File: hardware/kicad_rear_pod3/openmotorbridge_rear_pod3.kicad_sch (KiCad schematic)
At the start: 0 parts

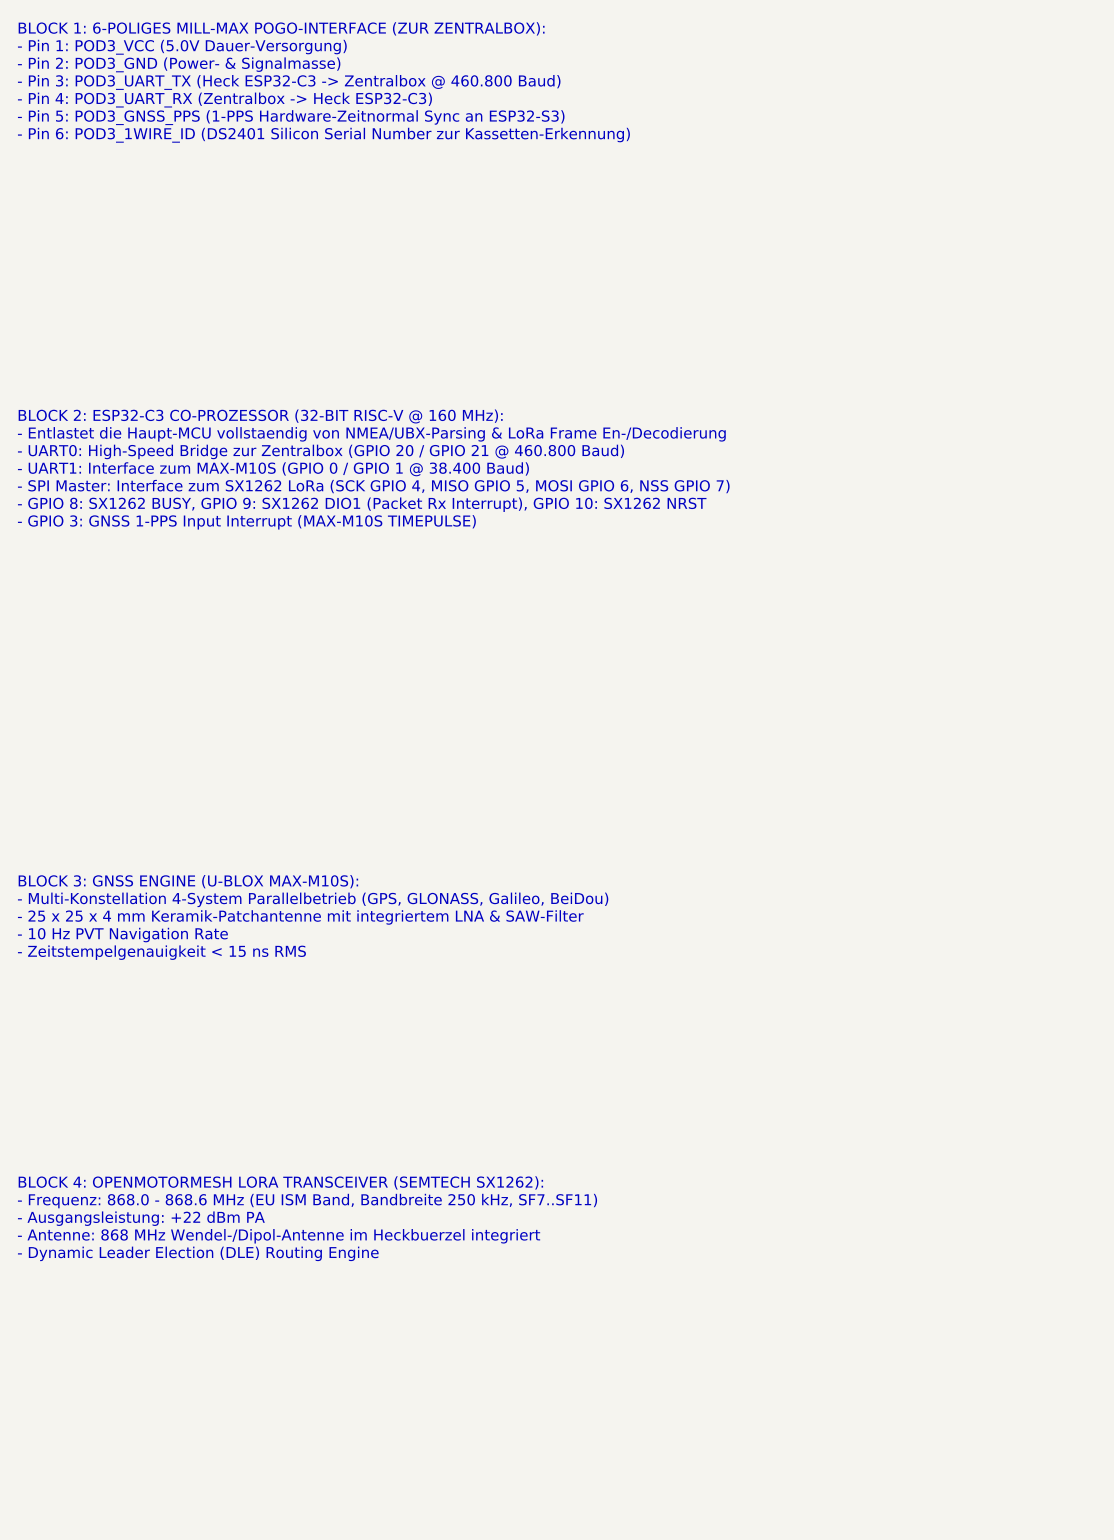
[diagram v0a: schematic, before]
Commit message: feat: Add Adaptive Tiered QoS, Dual-PHY OMM, Dead Reckoning, Actioncam Remote & i18n
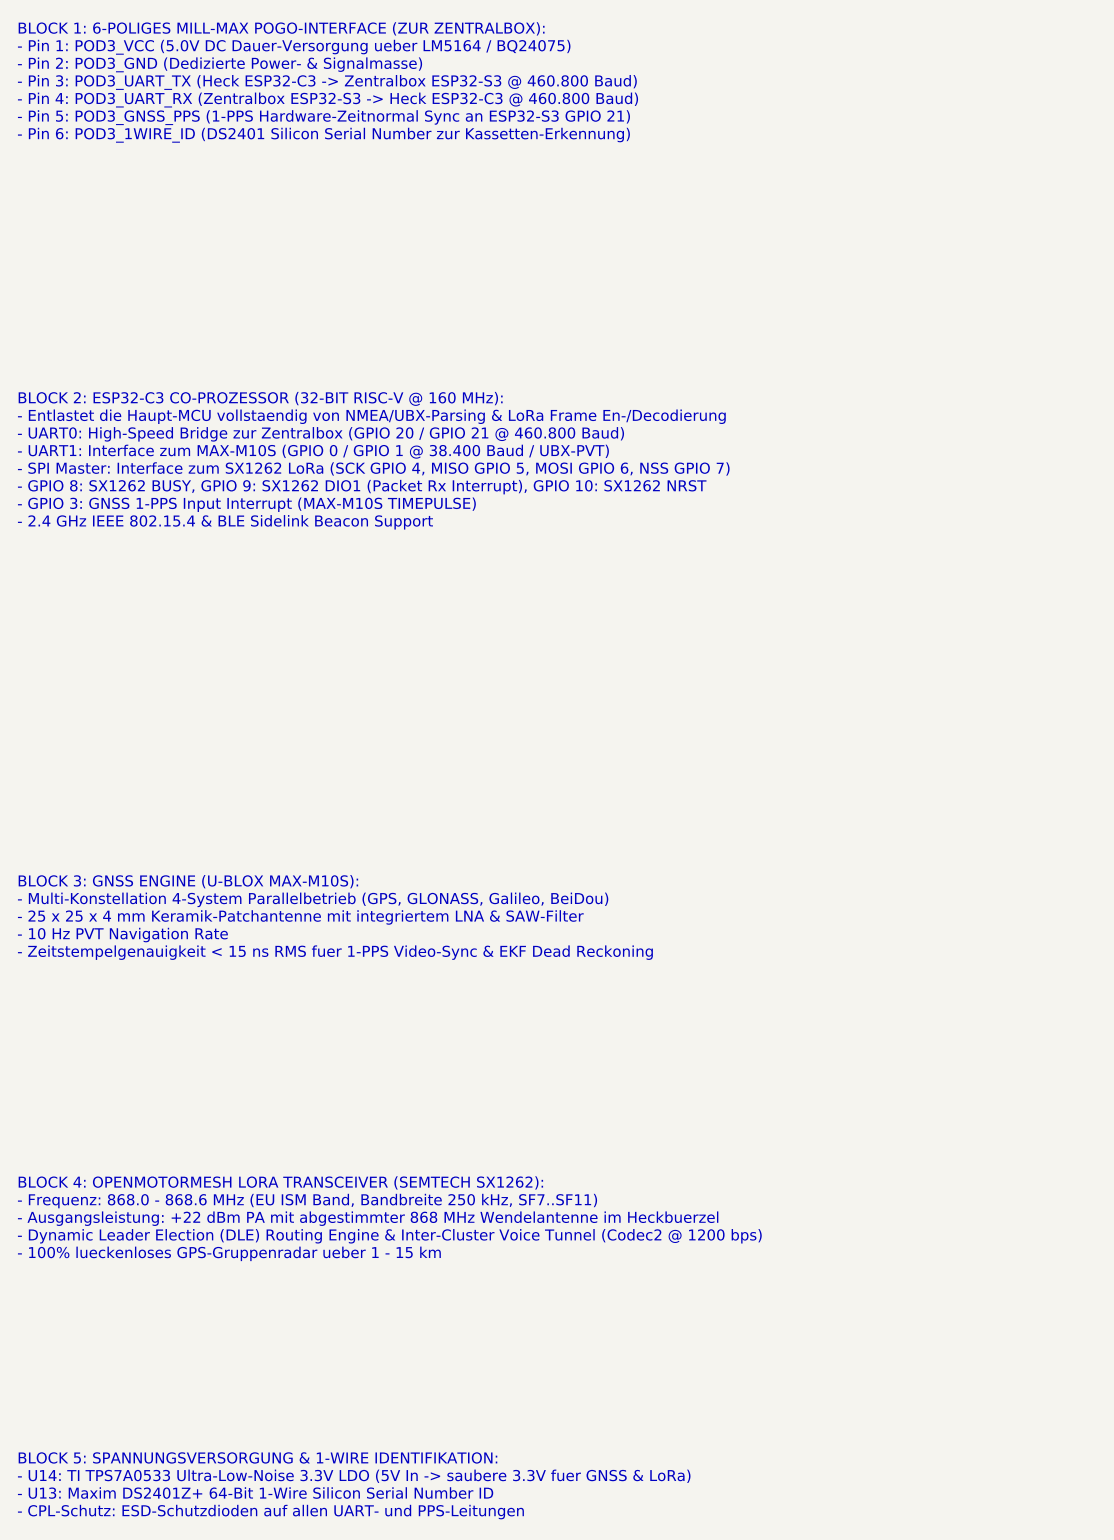
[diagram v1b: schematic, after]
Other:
- note added: "BLOCK 1: 6-POLIGES MILL-MAX POGO-INTERFACE (ZUR ZENTRALBOX): - Pin 1: POD3_VCC (5.0V DC Dauer-Versorgung ueber LM5164 / BQ24075) - Pin 2: POD3_GND (Dedizierte Power- & Signalmasse) - Pin 3: POD3_UART_TX (Heck ESP32-C3 -> Zentralbox ESP32-S3 @ 460.800 Baud) - Pin 4: POD3_UART_RX (Zentralbox ESP32-S3 -> Heck ESP32-C3 @ 460.800 Baud) - Pin 5: POD3_GNSS_PPS (1-PPS Hardware-Zeitnormal Sync an ESP32-S3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"
- note added: "BLOCK 2: ESP32-C3 CO-PROZESSOR (32-BIT RISC-V @ 160 MHz): - Entlastet die Haupt-MCU vollstaendig von NMEA/UBX-Parsing & LoRa Frame En-/Decodierung - UART0: High-Speed Bridge zur Zentralbox (GPIO 20 / GPIO 21 @ 460.800 Baud) - UART1: Interface zum MAX-M10S (GPIO 0 / GPIO 1 @ 38.400 Baud / UBX-PVT) - SPI Master: Interface zum SX1262 LoRa (SCK GPIO 4, MISO GPIO 5, MOSI GPIO 6, NSS GPIO 7) - GPIO 8: 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"
- note added: "BLOCK 3: GNSS ENGINE (U-BLOX MAX-M10S): - Multi-Konstellation 4-System Parallelbetrieb (GPS, GLONASS, Galileo, BeiDou) - 25 x 25 x 4 mm Keramik-Patchantenne mit integriertem LNA & SAW-Filter - 10 Hz PVT Navigation Rate - Zeitstempelgenauigkeit < 15 ns RMS fuer 1-PPS Video-Sync & EKF Dead Reckoning"
- note added: "BLOCK 4: OPENMOTORMESH LORA TRANSCEIVER (SEMTECH SX1262): - Frequenz: 868.0 - 868.6 MHz (EU ISM Band, Bandbreite 250 kHz, SF7..SF11) - Ausgangsleistung: +22 dBm PA mit abgestimmter 868 MHz Wendelantenne im Heckbuerzel - Dynamic Leader Election (DLE) Routing Engine & Inter-Cluster Voice Tunnel (Codec2 @ 1200 bps) - 100% lueckenloses GPS-Gruppenradar ueber 1 - 15 km"
- note added: "BLOCK 5: SPANNUNGSVERSORGUNG & 1-WIRE IDENTIFIKATION: - U14: TI TPS7A0533 Ultra-Low-Noise 3.3V LDO (5V In -> saubere 3.3V fuer GNSS & LoRa) - U13: Maxim DS2401Z+ 64-Bit 1-Wire Silicon Serial Number ID - CPL-Schutz: ESD-Schutzdioden auf allen UART- und PPS-Leitungen"
- note removed: "BLOCK 1: 6-POLIGES MILL-MAX POGO-INTERFACE (ZUR ZENTRALBOX): - Pin 1: POD3_VCC (5.0V Dauer-Versorgung) - Pin 2: POD3_GND (Power- & Signalmasse) - Pin 3: POD3_UART_TX (Heck ESP32-C3 -> Zentralbox @ 460.800 Baud) - Pin 4: POD3_UART_RX (Zentralbox -> Heck ESP32-C3) - Pin 5: POD3_GNSS_PPS (1-PPS Hardware-Zeitnormal Sync an ESP32-S3) - Pin 6: POD3_1WIRE_ID (DS2401 Silicon Serial Number zur Kassetten-E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"
- note removed: "BLOCK 2: ESP32-C3 CO-PROZESSOR (32-BIT RISC-V @ 160 MHz): - Entlastet die Haupt-MCU vollstaendig von NMEA/UBX-Parsing & LoRa Frame En-/Decodierung - UART0: High-Speed Bridge zur Zentralbox (GPIO 20 / GPIO 21 @ 460.800 Baud) - UART1: Interface zum MAX-M10S (GPIO 0 / GPIO 1 @ 38.400 Baud) - SPI Master: Interface zum SX1262 LoRa (SCK GPIO 4, MISO GPIO 5, MOSI GPIO 6, NSS GPIO 7) - GPIO 8: SX1262 BUS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"
- note removed: "BLOCK 3: GNSS ENGINE (U-BLOX MAX-M10S): - Multi-Konstellation 4-System Parallelbetrieb (GPS, GLONASS, Galileo, BeiDou) - 25 x 25 x 4 mm Keramik-Patchantenne mit integriertem LNA & SAW-Filter - 10 Hz PVT Navigation Rate - Zeitstempelgenauigkeit < 15 ns RMS"
- note removed: "BLOCK 4: OPENMOTORMESH LORA TRANSCEIVER (SEMTECH SX1262): - Frequenz: 868.0 - 868.6 MHz (EU ISM Band, Bandbreite 250 kHz, SF7..SF11) - Ausgangsleistung: +22 dBm PA - Antenne: 868 MHz Wendel-/Dipol-Antenne im Heckbuerzel integriert - Dynamic Leader Election (DLE) Routing Engine"
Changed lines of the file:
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@@
     (comment 2 "ESP32-C3 RISC-V Co-Prozessor + DS2401 1-Wire ID + 6-Pin Pogo Interface")
   )
-  (text "BLOCK 1: 6-POLIGES MILL-MAX POGO-INTERFACE (ZUR ZENTRALBOX):\n- Pin 1: POD3_VCC (5.0V Dauer-Versorgung)\n- Pin 2: POD3_GND (Power- & Signalmasse)\n- Pin 3: POD3_UART_TX (Heck ESP32-C3 -> Zentralbox @ 460.800 Baud)\n- Pin 4: POD3_UART_RX (Zentralbox -> Heck ESP32-C3)\n- Pin 5: POD3_GNSS_PPS (1-PPS Hardware-Zeitnormal Sync an ESP32-S3)\n- Pin 6: POD3_1WIRE_ID (DS2401 Silicon Serial Number zur Kassetten-Erkennung)" (at 25.4 45.0 0)
+  (text "BLOCK 1: 6-POLIGES MILL-MAX POGO-INTERFACE (ZUR ZENTRALBOX):\n- Pin 1: POD3_VCC (5.0V DC Dauer-Versorgung ueber LM5164 / BQ24075)\n- Pin 2: POD3_GND (Dedizierte Power- & Signalmasse)\n- Pin 3: POD3_UART_TX (Heck ESP32-C3 -> Zentralbox ESP32-S3 @ 460.800 Baud)\n- Pin 4: POD3_UART_RX (Zentralbox ESP32-S3 -> Heck ESP32-C3 @ 460.800 Baud)\n- Pin 5: POD3_GNSS_PPS (1-PPS Hardware-Zeitnormal Sync an ESP32-S3 GPIO 21)\n- Pin 6: POD3_1WIRE_ID (DS2401 Silicon Serial Number zur Kassetten-Erkennung)" (at 25.4 45.0 0)
     (effects (font (size 1.27 1.27)) (justify left bottom))
   )
-  (text "BLOCK 2: ESP32-C3 CO-PROZESSOR (32-BIT RISC-V @ 160 MHz):\n- Entlastet die Haupt-MCU vollstaendig von NMEA/UBX-Parsing & LoRa Frame En-/Decodierung\n- UART0: High-Speed Bridge zur Zentralbox (GPIO 20 / GPIO 21 @ 460.800 Baud)\n- UART1: Interface zum MAX-M10S (GPIO 0 / GPIO 1 @ 38.400 Baud)\n- SPI Master: Interface zum SX1262 LoRa (SCK GPIO 4, MISO GPIO 5, MOSI GPIO 6, NSS GPIO 7)\n- GPIO 8: SX1262 BUSY, GPIO 9: SX1262 DIO1 (Packet Rx Interrupt), GPIO 10: SX1262 NRST\n- GPIO 3: GNSS 1-PPS Input Interrupt (MAX-M10S TIMEPULSE)" (at 25.4 90.0 0)
+  (text "BLOCK 2: ESP32-C3 CO-PROZESSOR (32-BIT RISC-V @ 160 MHz):\n- Entlastet die Haupt-MCU vollstaendig von NMEA/UBX-Parsing & LoRa Frame En-/Decodierung\n- UART0: High-Speed Bridge zur Zentralbox (GPIO 20 / GPIO 21 @ 460.800 Baud)\n- UART1: Interface zum MAX-M10S (GPIO 0 / GPIO 1 @ 38.400 Baud / UBX-PVT)\n- SPI Master: Interface zum SX1262 LoRa (SCK GPIO 4, MISO GPIO 5, MOSI GPIO 6, NSS GPIO 7)\n- GPIO 8: SX1262 BUSY, GPIO 9: SX1262 DIO1 (Packet Rx Interrupt), GPIO 10: SX1262 NRST\n- GPIO 3: GNSS 1-PPS Input Interrupt (MAX-M10S TIMEPULSE)\n- 2.4 GHz IEEE 802.15.4 & BLE Sidelink Beacon Support" (at 25.4 90.0 0)
     (effects (font (size 1.27 1.27)) (justify left bottom))
   )
-  (text "BLOCK 3: GNSS ENGINE (U-BLOX MAX-M10S):\n- Multi-Konstellation 4-System Parallelbetrieb (GPS, GLONASS, Galileo, BeiDou)\n- 25 x 25 x 4 mm Keramik-Patchantenne mit integriertem LNA & SAW-Filter\n- 10 Hz PVT Navigation Rate\n- Zeitstempelgenauigkeit < 15 ns RMS" (at 25.4 140.0 0)
+  (text "BLOCK 3: GNSS ENGINE (U-BLOX MAX-M10S):\n- Multi-Konstellation 4-System Parallelbetrieb (GPS, GLONASS, Galileo, BeiDou)\n- 25 x 25 x 4 mm Keramik-Patchantenne mit integriertem LNA & SAW-Filter\n- 10 Hz PVT Navigation Rate\n- Zeitstempelgenauigkeit < 15 ns RMS fuer 1-PPS Video-Sync & EKF Dead Reckoning" (at 25.4 140.0 0)
     (effects (font (size 1.27 1.27)) (justify left bottom))
   )
-  (text "BLOCK 4: OPENMOTORMESH LORA TRANSCEIVER (SEMTECH SX1262):\n- Frequenz: 868.0 - 868.6 MHz (EU ISM Band, Bandbreite 250 kHz, SF7..SF11)\n- Ausgangsleistung: +22 dBm PA\n- Antenne: 868 MHz Wendel-/Dipol-Antenne im Heckbuerzel integriert\n- Dynamic Leader Election (DLE) Routing Engine" (at 25.4 175.0 0)
+  (text "BLOCK 4: OPENMOTORMESH LORA TRANSCEIVER (SEMTECH SX1262):\n- Frequenz: 868.0 - 868.6 MHz (EU ISM Band, Bandbreite 250 kHz, SF7..SF11)\n- Ausgangsleistung: +22 dBm PA mit abgestimmter 868 MHz Wendelantenne im Heckbuerzel\n- Dynamic Leader Election (DLE) Routing Engine & Inter-Cluster Voice Tunnel (Codec2 @ 1200 bps)\n- 100% lueckenloses GPS-Gruppenradar ueber 1 - 15 km" (at 25.4 175.0 0)
     (effects (font (size 1.27 1.27)) (justify left bottom))
   )
+  (text "BLOCK 5: SPANNUNGSVERSORGUNG & 1-WIRE IDENTIFIKATION:\n- U14: TI TPS7A0533 Ultra-Low-Noise 3.3V LDO (5V In -> saubere 3.3V fuer GNSS & LoRa)\n- U13: Maxim DS2401Z+ 64-Bit 1-Wire Silicon Serial Number ID\n- CPL-Schutz: ESD-Schutzdioden auf allen UART- und PPS-Leitungen" (at 25.4 205.0 0)
+    (effects (font (size 1.27 1.27)) (justify left bottom))
+  )
